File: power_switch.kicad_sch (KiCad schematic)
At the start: 16 parts, among them J1 Power Output, U1 BTS7004-1EPP

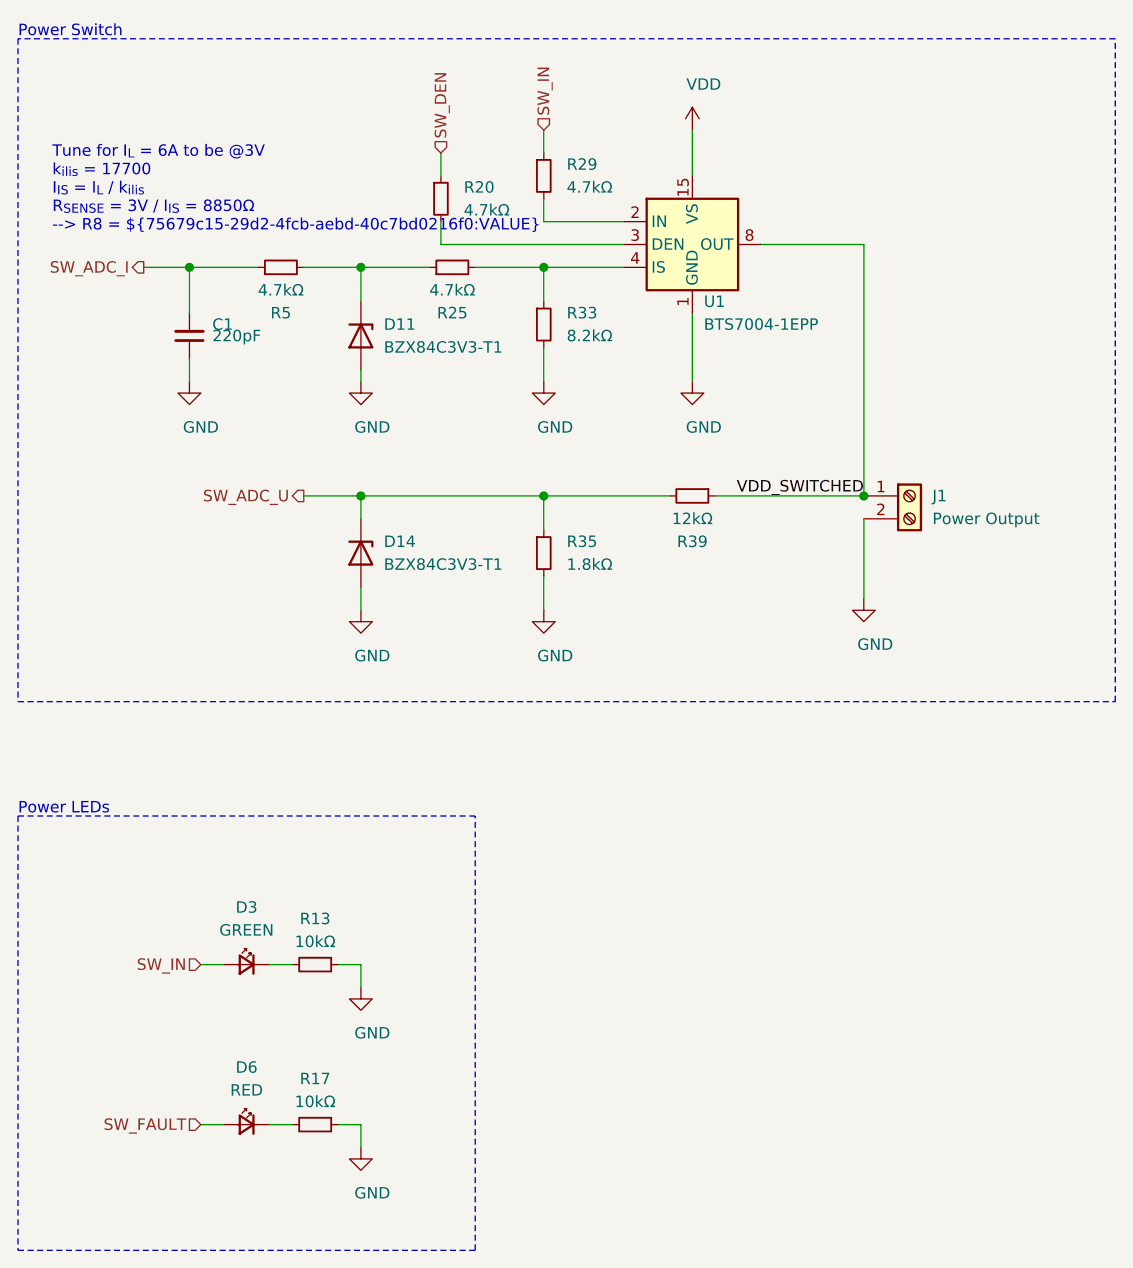
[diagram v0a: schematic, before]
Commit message: place decoupling capacitors nicer, add USB ESD protection
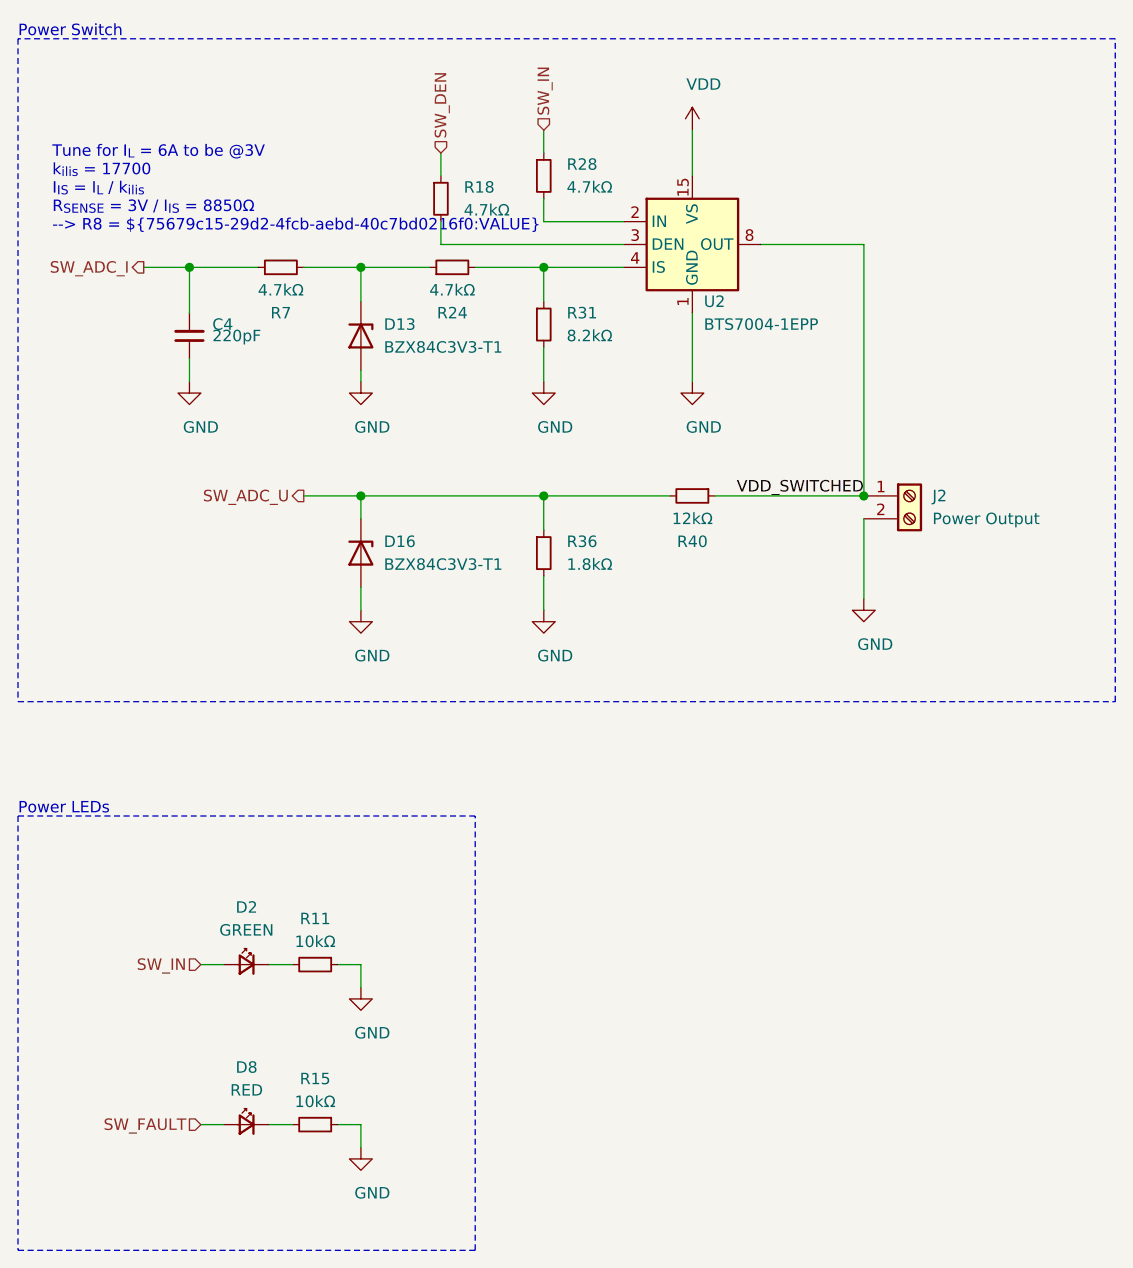
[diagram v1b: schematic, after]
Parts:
- renumbered C1 to C4, D11 to D13, D14 to D16, D3 to D2, D6 to D8, J1 to J2, R13 to R11, R17 to R15, R20 to R18, R25 to R24, R29 to R28, R33 to R31, R35 to R36, R39 to R40, R5 to R7, U1 to U2
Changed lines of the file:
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@@
   (symbol (lib_id "power:VDD") (at 93.98 29.21 0)
     (in_bom yes) (on_board yes)
-    (property "Reference" "#PWR045" (id 0) (at 93.98 33.02 0)
+    (property "Reference" "#PWR044" (id 0) (at 93.98 33.02 0)
       (effects (font (size 1.27 1.27)) hide)
     )
@@
   (symbol (lib_id "power:GND") (at 38.1 57.15 0)
     (in_bom yes) (on_board yes)
-    (property "Reference" "#PWR09" (id 0) (at 38.1 63.5 0)
+    (property "Reference" "#PWR07" (id 0) (at 38.1 63.5 0)
       (effects (font (size 1.27 1.27)) hide)
     )
@@
   (symbol (lib_id "power:GND") (at 57.15 57.15 0)
     (in_bom yes) (on_board yes)
-    (property "Reference" "#PWR021" (id 0) (at 57.15 63.5 0)
+    (property "Reference" "#PWR018" (id 0) (at 57.15 63.5 0)
       (effects (font (size 1.27 1.27)) hide)
     )
@@
   (symbol (lib_id "power:GND") (at 57.15 82.55 0)
     (in_bom yes) (on_board yes)
-    (property "Reference" "#PWR023" (id 0) (at 57.15 88.9 0)
+    (property "Reference" "#PWR024" (id 0) (at 57.15 88.9 0)
       (effects (font (size 1.27 1.27)) hide)
     )
@@
   (symbol (lib_id "power:GND") (at 57.15 124.46 0)
     (in_bom yes) (on_board yes)
-    (property "Reference" "#PWR028" (id 0) (at 57.15 130.81 0)
+    (property "Reference" "#PWR026" (id 0) (at 57.15 130.81 0)
       (effects (font (size 1.27 1.27)) hide)
     )
@@
   (symbol (lib_id "power:GND") (at 57.15 142.24 0)
     (in_bom yes) (on_board yes)
-    (property "Reference" "#PWR032" (id 0) (at 57.15 148.59 0)
+    (property "Reference" "#PWR030" (id 0) (at 57.15 148.59 0)
       (effects (font (size 1.27 1.27)) hide)
     )
@@
   (symbol (lib_id "power:GND") (at 77.47 57.15 0)
     (in_bom yes) (on_board yes)
-    (property "Reference" "#PWR038" (id 0) (at 77.47 63.5 0)
+    (property "Reference" "#PWR035" (id 0) (at 77.47 63.5 0)
       (effects (font (size 1.27 1.27)) hide)
     )
@@
   (symbol (lib_id "power:GND") (at 77.47 82.55 0)
     (in_bom yes) (on_board yes)
-    (property "Reference" "#PWR041" (id 0) (at 77.47 88.9 0)
+    (property "Reference" "#PWR040" (id 0) (at 77.47 88.9 0)
       (effects (font (size 1.27 1.27)) hide)
     )
@@
   (symbol (lib_id "power:GND") (at 93.98 57.15 0)
     (in_bom yes) (on_board yes)
-    (property "Reference" "#PWR049" (id 0) (at 93.98 63.5 0)
+    (property "Reference" "#PWR048" (id 0) (at 93.98 63.5 0)
       (effects (font (size 1.27 1.27)) hide)
     )
@@
   (symbol (lib_id "power:GND") (at 113.03 81.28 0)
     (in_bom yes) (on_board yes)
-    (property "Reference" "#PWR054" (id 0) (at 113.03 87.63 0)
+    (property "Reference" "#PWR056" (id 0) (at 113.03 87.63 0)
       (effects (font (size 1.27 1.27)) hide)
     )
@@
   (symbol (lib_id "Device:R_Small") (at 48.26 44.45 90)
     (in_bom yes) (on_board yes)
-    (property "Reference" "R5" (id 0) (at 48.26 49.53 90))
+    (property "Reference" "R7" (id 0) (at 48.26 49.53 90))
     (property "Value" "4.7kΩ" (id 1) (at 48.26 46.99 90))
     (property "Footprint" "Resistor_SMD:R_0603_1608Metric" (id 2) (at 48.26 46.228 90)
@@
   (symbol (lib_id "Device:R_Small") (at 52.07 121.92 270)
     (in_bom yes) (on_board yes)
-    (property "Reference" "R13" (id 0) (at 52.07 116.84 90))
+    (property "Reference" "R11" (id 0) (at 52.07 116.84 90))
     (property "Value" "10kΩ" (id 1) (at 52.07 119.38 90))
     (property "Footprint" "Resistor_SMD:R_0603_1608Metric" (id 2) (at 52.07 120.142 90)
@@
   (symbol (lib_id "Device:R_Small") (at 52.07 139.7 270)
     (in_bom yes) (on_board yes)
-    (property "Reference" "R17" (id 0) (at 52.07 134.62 90))
+    (property "Reference" "R15" (id 0) (at 52.07 134.62 90))
     (property "Value" "10kΩ" (id 1) (at 52.07 137.16 90))
     (property "Footprint" "Resistor_SMD:R_0603_1608Metric" (id 2) (at 52.07 137.922 90)
@@
   (symbol (lib_id "Device:R_Small") (at 66.04 36.83 0)
     (in_bom yes) (on_board yes)
-    (property "Reference" "R20" (id 0) (at 68.58 35.56 0)
+    (property "Reference" "R18" (id 0) (at 68.58 35.56 0)
       (effects (font (size 1.27 1.27)) (justify left))
     )
@@
   (symbol (lib_id "Device:R_Small") (at 67.31 44.45 90)
     (in_bom yes) (on_board yes)
-    (property "Reference" "R25" (id 0) (at 67.31 49.53 90))
+    (property "Reference" "R24" (id 0) (at 67.31 49.53 90))
     (property "Value" "4.7kΩ" (id 1) (at 67.31 46.99 90))
     (property "Footprint" "Resistor_SMD:R_0603_1608Metric" (id 2) (at 67.31 46.228 90)
@@
   (symbol (lib_id "Device:R_Small") (at 77.47 34.29 0)
     (in_bom yes) (on_board yes)
-    (property "Reference" "R29" (id 0) (at 80.01 33.02 0)
+    (property "Reference" "R28" (id 0) (at 80.01 33.02 0)
       (effects (font (size 1.27 1.27)) (justify left))
     )
@@
   (symbol (lib_id "Device:R_Small") (at 77.47 50.8 0)
     (in_bom yes) (on_board yes)
-    (property "Reference" "R33" (id 0) (at 80.01 49.53 0)
+    (property "Reference" "R31" (id 0) (at 80.01 49.53 0)
       (effects (font (size 1.27 1.27)) (justify left))
     )
@@
   (symbol (lib_id "Device:R_Small") (at 77.47 76.2 0)
     (in_bom yes) (on_board yes)
-    (property "Reference" "R35" (id 0) (at 80.01 74.93 0)
+    (property "Reference" "R36" (id 0) (at 80.01 74.93 0)
       (effects (font (size 1.27 1.27)) (justify left))
     )
@@
   (symbol (lib_id "Device:R_Small") (at 93.98 69.85 270)
     (in_bom yes) (on_board yes)
-    (property "Reference" "R39" (id 0) (at 93.98 74.93 90))
+    (property "Reference" "R40" (id 0) (at 93.98 74.93 90))
     (property "Value" "12kΩ" (id 1) (at 93.98 72.39 90))
     (property "Footprint" "Resistor_SMD:R_0603_1608Metric" (id 2) (at 93.98 69.85 0)
@@
   (symbol (lib_id "Device:LED_Small") (at 44.45 121.92 0) (mirror y)
     (in_bom yes) (on_board yes)
-    (property "Reference" "D3" (id 0) (at 44.45 115.57 0))
+    (property "Reference" "D2" (id 0) (at 44.45 115.57 0))
     (property "Value" "GREEN" (id 1) (at 44.45 118.11 0))
     (property "Footprint" "LED_SMD:LED_0603_1608Metric" (id 2) (at 44.45 121.92 90)
@@
   (symbol (lib_id "Device:LED_Small") (at 44.45 139.7 0) (mirror y)
     (in_bom yes) (on_board yes)
-    (property "Reference" "D6" (id 0) (at 44.45 133.35 0))
+    (property "Reference" "D8" (id 0) (at 44.45 133.35 0))
     (property "Value" "RED" (id 1) (at 44.45 135.89 0))
     (property "Footprint" "LED_SMD:LED_0603_1608Metric" (id 2) (at 44.45 139.7 90)
@@
   (symbol (lib_id "Device:C_Small") (at 38.1 52.07 180)
     (in_bom yes) (on_board yes)
-    (property "Reference" "C1" (id 0) (at 40.64 50.8 0)
+    (property "Reference" "C4" (id 0) (at 40.64 50.8 0)
       (effects (font (size 1.27 1.27)) (justify right))
     )
@@
   (symbol (lib_id "Diode:DZ2S033X0L") (at 57.15 52.07 270)
     (in_bom yes) (on_board yes)
-    (property "Reference" "D11" (id 0) (at 59.69 50.8 90)
+    (property "Reference" "D13" (id 0) (at 59.69 50.8 90)
       (effects (font (size 1.27 1.27)) (justify left))
     )
@@
   (symbol (lib_id "Diode:DZ2S033X0L") (at 57.15 76.2 270)
     (in_bom yes) (on_board yes)
-    (property "Reference" "D14" (id 0) (at 59.69 74.93 90)
+    (property "Reference" "D16" (id 0) (at 59.69 74.93 90)
       (effects (font (size 1.27 1.27)) (justify left))
     )
@@
   (symbol (lib_id "Connector:Screw_Terminal_01x02") (at 118.11 69.85 0)
     (in_bom yes) (on_board yes)
-    (property "Reference" "J1" (id 0) (at 120.65 69.85 0)
+    (property "Reference" "J2" (id 0) (at 120.65 69.85 0)
       (effects (font (size 1.27 1.27)) (justify left))
     )
@@
   (symbol (lib_id "Power_Management:BTS7004-1EPP") (at 93.98 41.91 0)
     (in_bom yes) (on_board yes)
-    (property "Reference" "U1" (id 0) (at 95.25 48.26 0)
-      (effects (font (size 1.27 1.27)) (justify left))
-    )
+    (property "Reference" "U2" (id 0) (at 95.25 48.26 0)
+      (effects (font (size 1.27 1.27)) (justify left))
+    )

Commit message: layouting finished, some microcontroller connection rearrangements
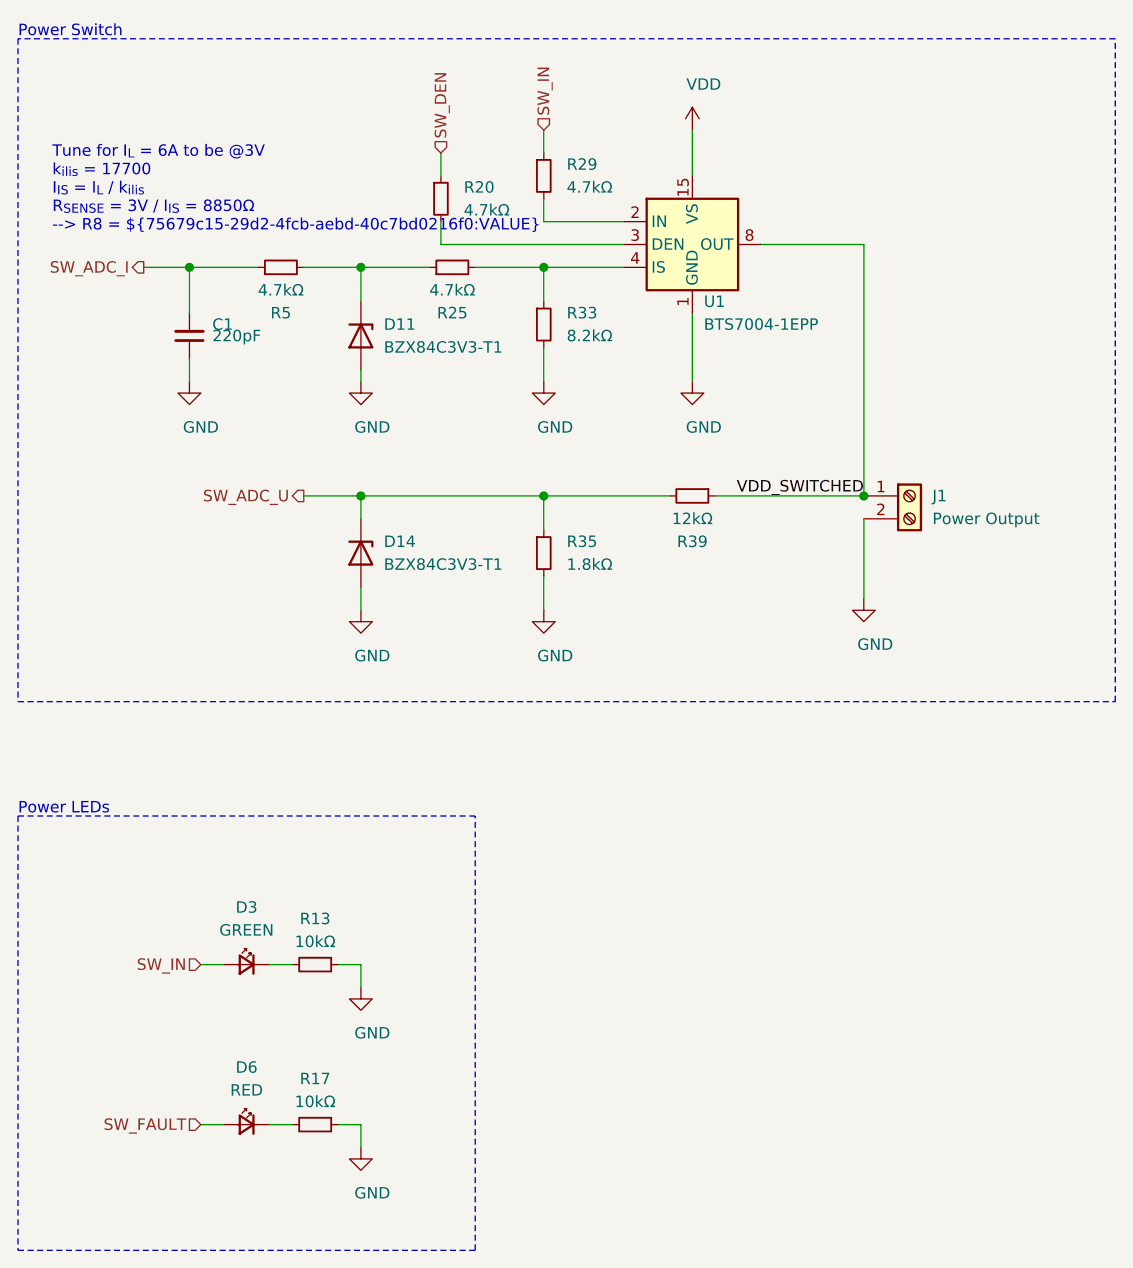
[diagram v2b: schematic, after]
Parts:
- renumbered C4 to C1, D13 to D11, D16 to D14, D2 to D3, D8 to D6, J2 to J1, R11 to R13, R15 to R17, R18 to R20, R24 to R25, R28 to R29, R31 to R33, R36 to R35, R40 to R39, R7 to R5, U2 to U1
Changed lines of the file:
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@@
   (symbol (lib_id "Device:R_Small") (at 48.26 44.45 90)
     (in_bom yes) (on_board yes)
-    (property "Reference" "R7" (id 0) (at 48.26 49.53 90))
+    (property "Reference" "R5" (id 0) (at 48.26 49.53 90))
     (property "Value" "4.7kΩ" (id 1) (at 48.26 46.99 90))
     (property "Footprint" "Resistor_SMD:R_0603_1608Metric" (id 2) (at 48.26 46.228 90)
@@
   (symbol (lib_id "Device:R_Small") (at 52.07 121.92 270)
     (in_bom yes) (on_board yes)
-    (property "Reference" "R11" (id 0) (at 52.07 116.84 90))
+    (property "Reference" "R13" (id 0) (at 52.07 116.84 90))
     (property "Value" "10kΩ" (id 1) (at 52.07 119.38 90))
     (property "Footprint" "Resistor_SMD:R_0603_1608Metric" (id 2) (at 52.07 120.142 90)
@@
   (symbol (lib_id "Device:R_Small") (at 52.07 139.7 270)
     (in_bom yes) (on_board yes)
-    (property "Reference" "R15" (id 0) (at 52.07 134.62 90))
+    (property "Reference" "R17" (id 0) (at 52.07 134.62 90))
     (property "Value" "10kΩ" (id 1) (at 52.07 137.16 90))
     (property "Footprint" "Resistor_SMD:R_0603_1608Metric" (id 2) (at 52.07 137.922 90)
@@
   (symbol (lib_id "Device:R_Small") (at 66.04 36.83 0)
     (in_bom yes) (on_board yes)
-    (property "Reference" "R18" (id 0) (at 68.58 35.56 0)
+    (property "Reference" "R20" (id 0) (at 68.58 35.56 0)
       (effects (font (size 1.27 1.27)) (justify left))
     )
@@
   (symbol (lib_id "Device:R_Small") (at 67.31 44.45 90)
     (in_bom yes) (on_board yes)
-    (property "Reference" "R24" (id 0) (at 67.31 49.53 90))
+    (property "Reference" "R25" (id 0) (at 67.31 49.53 90))
     (property "Value" "4.7kΩ" (id 1) (at 67.31 46.99 90))
     (property "Footprint" "Resistor_SMD:R_0603_1608Metric" (id 2) (at 67.31 46.228 90)
@@
   (symbol (lib_id "Device:R_Small") (at 77.47 34.29 0)
     (in_bom yes) (on_board yes)
-    (property "Reference" "R28" (id 0) (at 80.01 33.02 0)
+    (property "Reference" "R29" (id 0) (at 80.01 33.02 0)
       (effects (font (size 1.27 1.27)) (justify left))
     )
@@
   (symbol (lib_id "Device:R_Small") (at 77.47 50.8 0)
     (in_bom yes) (on_board yes)
-    (property "Reference" "R31" (id 0) (at 80.01 49.53 0)
+    (property "Reference" "R33" (id 0) (at 80.01 49.53 0)
       (effects (font (size 1.27 1.27)) (justify left))
     )
@@
   (symbol (lib_id "Device:R_Small") (at 77.47 76.2 0)
     (in_bom yes) (on_board yes)
-    (property "Reference" "R36" (id 0) (at 80.01 74.93 0)
+    (property "Reference" "R35" (id 0) (at 80.01 74.93 0)
       (effects (font (size 1.27 1.27)) (justify left))
     )
@@
   (symbol (lib_id "Device:R_Small") (at 93.98 69.85 270)
     (in_bom yes) (on_board yes)
-    (property "Reference" "R40" (id 0) (at 93.98 74.93 90))
+    (property "Reference" "R39" (id 0) (at 93.98 74.93 90))
     (property "Value" "12kΩ" (id 1) (at 93.98 72.39 90))
     (property "Footprint" "Resistor_SMD:R_0603_1608Metric" (id 2) (at 93.98 69.85 0)
@@
   (symbol (lib_id "Device:LED_Small") (at 44.45 121.92 0) (mirror y)
     (in_bom yes) (on_board yes)
-    (property "Reference" "D2" (id 0) (at 44.45 115.57 0))
+    (property "Reference" "D3" (id 0) (at 44.45 115.57 0))
     (property "Value" "GREEN" (id 1) (at 44.45 118.11 0))
     (property "Footprint" "LED_SMD:LED_0603_1608Metric" (id 2) (at 44.45 121.92 90)
@@
   (symbol (lib_id "Device:LED_Small") (at 44.45 139.7 0) (mirror y)
     (in_bom yes) (on_board yes)
-    (property "Reference" "D8" (id 0) (at 44.45 133.35 0))
+    (property "Reference" "D6" (id 0) (at 44.45 133.35 0))
     (property "Value" "RED" (id 1) (at 44.45 135.89 0))
     (property "Footprint" "LED_SMD:LED_0603_1608Metric" (id 2) (at 44.45 139.7 90)
@@
   (symbol (lib_id "Device:C_Small") (at 38.1 52.07 180)
     (in_bom yes) (on_board yes)
-    (property "Reference" "C4" (id 0) (at 40.64 50.8 0)
+    (property "Reference" "C1" (id 0) (at 40.64 50.8 0)
       (effects (font (size 1.27 1.27)) (justify right))
     )
@@
   (symbol (lib_id "Diode:DZ2S033X0L") (at 57.15 52.07 270)
     (in_bom yes) (on_board yes)
-    (property "Reference" "D13" (id 0) (at 59.69 50.8 90)
+    (property "Reference" "D11" (id 0) (at 59.69 50.8 90)
       (effects (font (size 1.27 1.27)) (justify left))
     )
@@
   (symbol (lib_id "Diode:DZ2S033X0L") (at 57.15 76.2 270)
     (in_bom yes) (on_board yes)
-    (property "Reference" "D16" (id 0) (at 59.69 74.93 90)
+    (property "Reference" "D14" (id 0) (at 59.69 74.93 90)
       (effects (font (size 1.27 1.27)) (justify left))
     )
@@
   (symbol (lib_id "Connector:Screw_Terminal_01x02") (at 118.11 69.85 0)
     (in_bom yes) (on_board yes)
-    (property "Reference" "J2" (id 0) (at 120.65 69.85 0)
+    (property "Reference" "J1" (id 0) (at 120.65 69.85 0)
       (effects (font (size 1.27 1.27)) (justify left))
     )
@@
   (symbol (lib_id "Power_Management:BTS7004-1EPP") (at 93.98 41.91 0)
     (in_bom yes) (on_board yes)
-    (property "Reference" "U2" (id 0) (at 95.25 48.26 0)
-      (effects (font (size 1.27 1.27)) (justify left))
-    )
+    (property "Reference" "U1" (id 0) (at 95.25 48.26 0)
+      (effects (font (size 1.27 1.27)) (justify left))
+    )
